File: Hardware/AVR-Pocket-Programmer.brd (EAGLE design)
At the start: 47 x 30.5 mm, 38 parts, among them Q1 12 MHz, U1 ATTINY2313-20S, U2 74ACT125D, X2 USBSMD

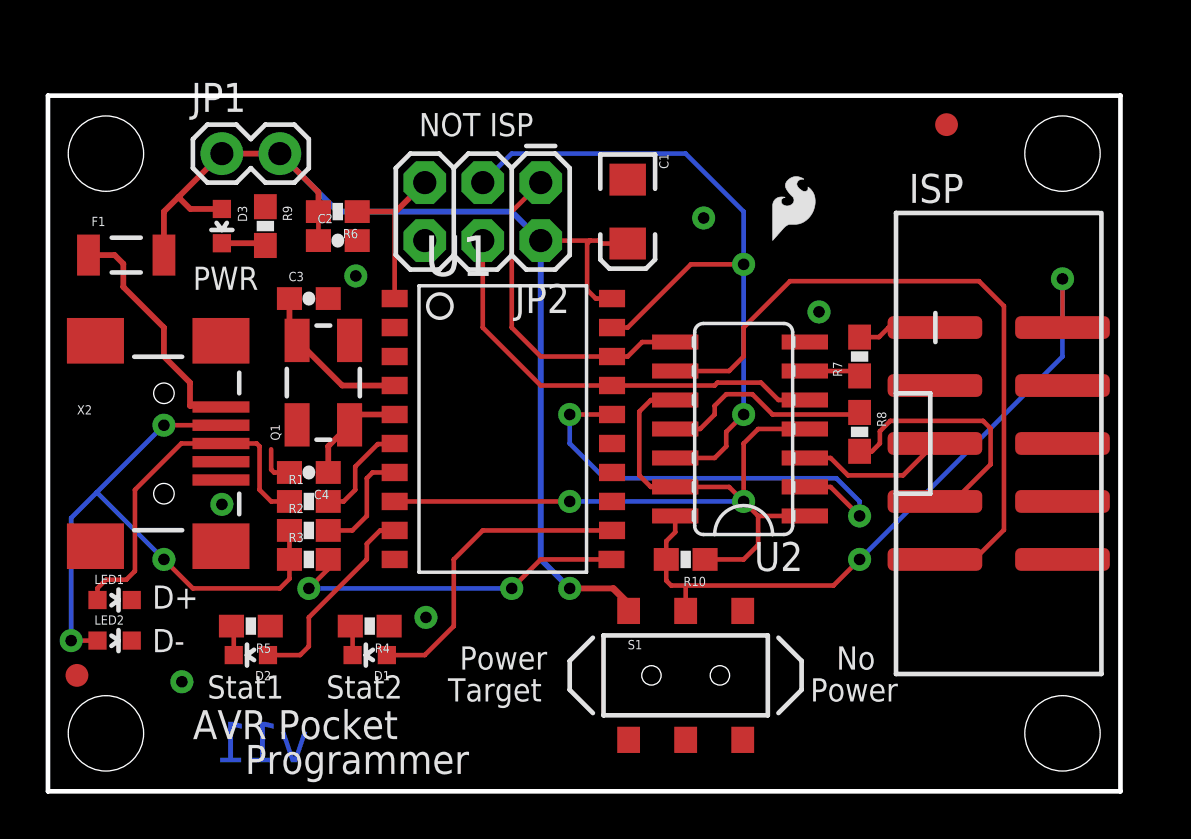
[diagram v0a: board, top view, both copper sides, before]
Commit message: Removed branding and updated docs
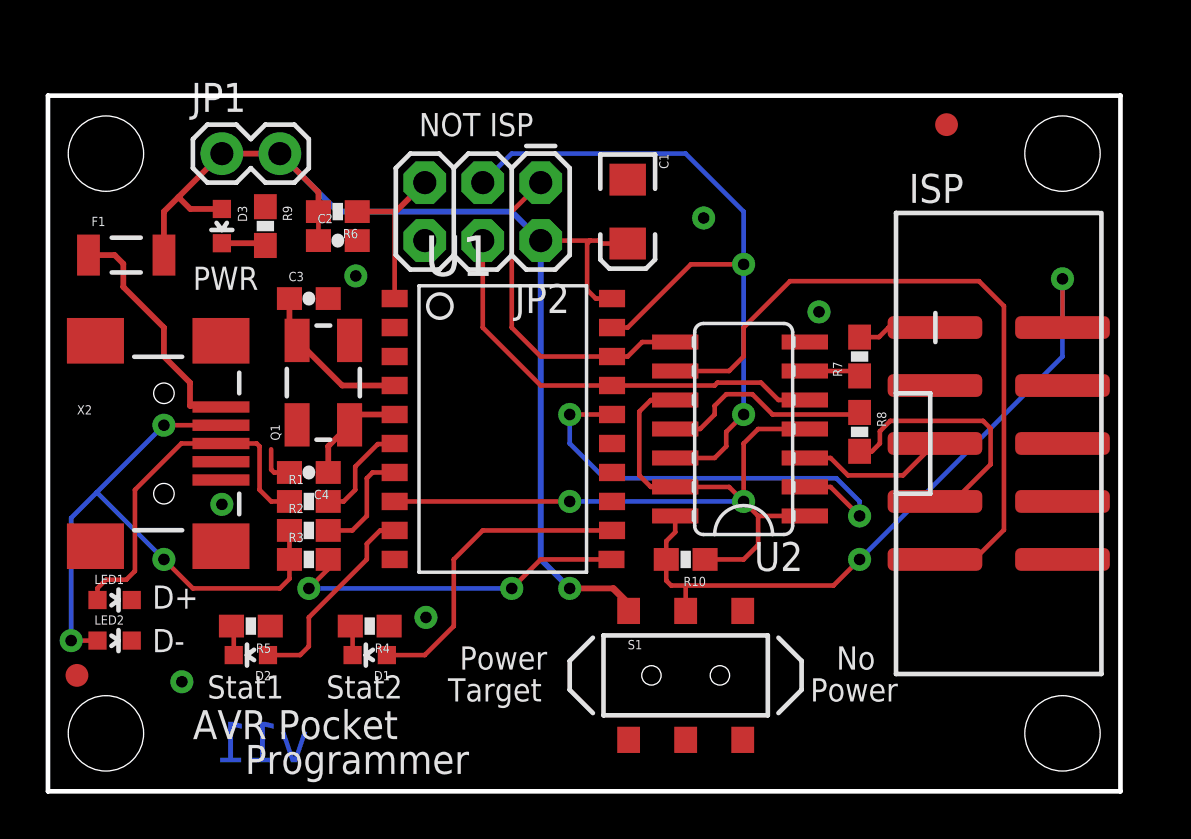
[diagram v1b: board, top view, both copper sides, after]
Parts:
- removed LOGO1: OSHW-LOGOM, SparkFun-Aesthetics:OSHW-LOGO-M
- removed U$2: LOGO-SFESK, SparkFun:SFE-LOGO-FLAME
- removed U$8: LOGO-SFENEW, SparkFun:SFE-NEW-WEBLOGO
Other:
- board text added: "Revision: Xavier Guay"
- board text removed: "Revision: Kade Jensen"

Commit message: Board Updated
- Resized and rounded edges
- Changed to USB Micro B
- Moved some wires to fit Error Check
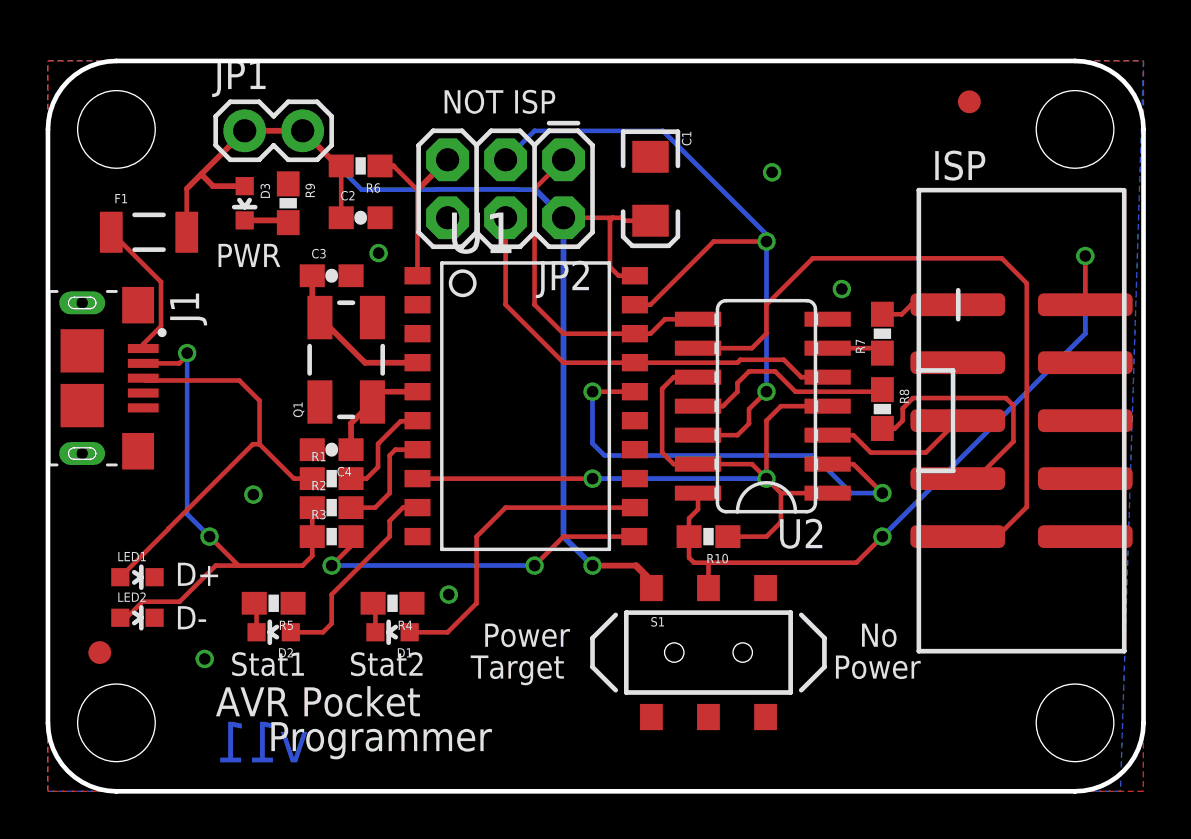
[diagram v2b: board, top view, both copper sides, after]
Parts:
- removed U$1, U$3, U$4, U$5: STAND-OFF, SparkFun:STAND-OFF
- removed X2: USBSMD, SparkFun:USB-MINIB
- added J1: 10118193-0001LF, USB-Micro:FCI_10118193-0001LF
- moved R6 2.24 mm to (13.7, 27.4)
- moved R8 1.41 mm to (36.6, 16.7)
- moved R4 1.41 mm to (15.1, 8.24)
- moved R5 1.41 mm to (9.89, 8.24)
- moved F1 1.41 mm to (4.43, 24.5)
- moved C1 1.41 mm to (26.4, 26.4)
- moved C2 1.41 mm to (13.7, 25.1)
- moved C3 1.41 mm to (12.4, 22.6)
- moved C4 1.41 mm to (12.4, 15.0)
- moved D1 1.41 mm to (15.1, 6.97)
- moved D2 1.41 mm to (9.89, 6.97)
- moved FRAME1 1.41 mm to (2.27, -10.4)
- moved JP2 1.41 mm to (22.6, 27.7)
- moved LED1 1.41 mm to (3.92, 9.38)
- moved LED2 1.41 mm to (3.92, 7.60)
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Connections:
- net D+: now also J1.3; no longer X2.D+
- net D-: now also J1.2; no longer X2.D-
- net GND: now also J1.5; no longer X2.GND
- net N$4: now also J1.1; no longer X2.VBUS
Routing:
- net N$4: track 10.8 -> 6.32 mm
- net D-: track 27.7 -> 24.1 mm, vias 3 -> 2
- net D+: track 15.8 -> 18.9 mm
- net GND: track 1.74 -> 0.00 mm
- net SCK': track 33.0 -> 31.8 mm
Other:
- board size 47 x 30.5 mm -> 48 x 32 mm
